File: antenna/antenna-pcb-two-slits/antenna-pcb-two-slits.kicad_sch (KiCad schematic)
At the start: 11 parts, among them J1 SMA Connector Male, U1 HHM1589D1

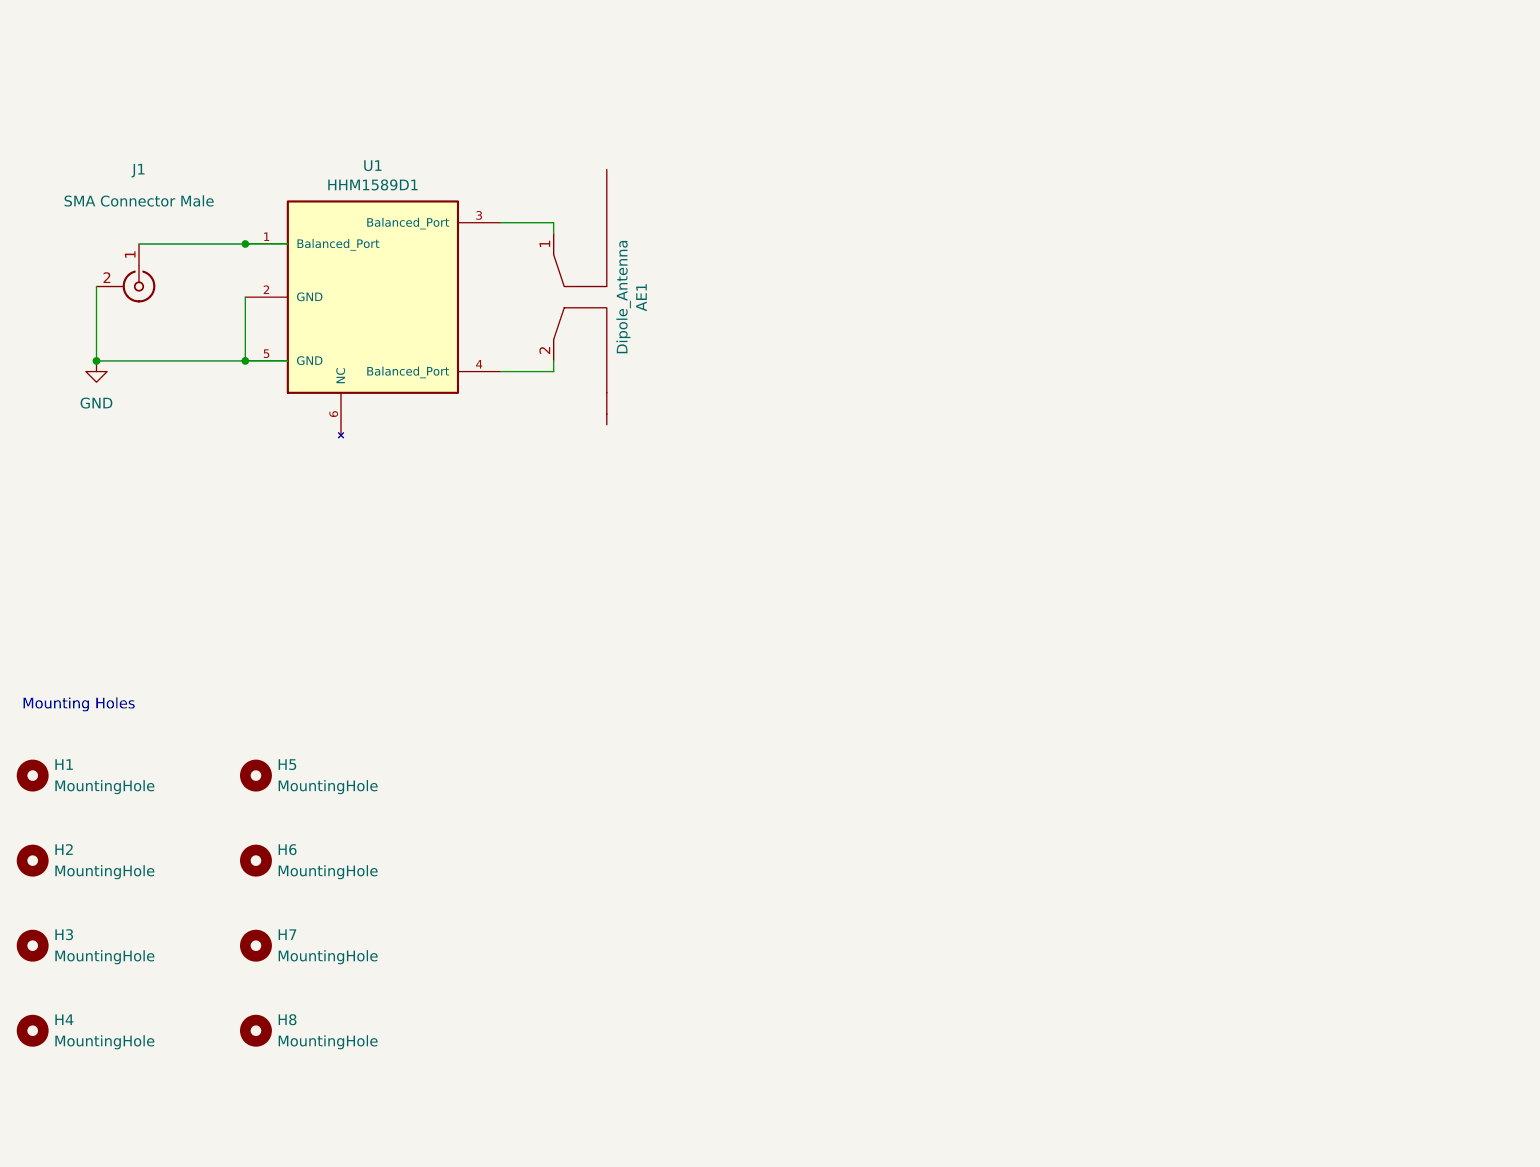
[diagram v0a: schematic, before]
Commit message: modify antenna pcbs and drc checked
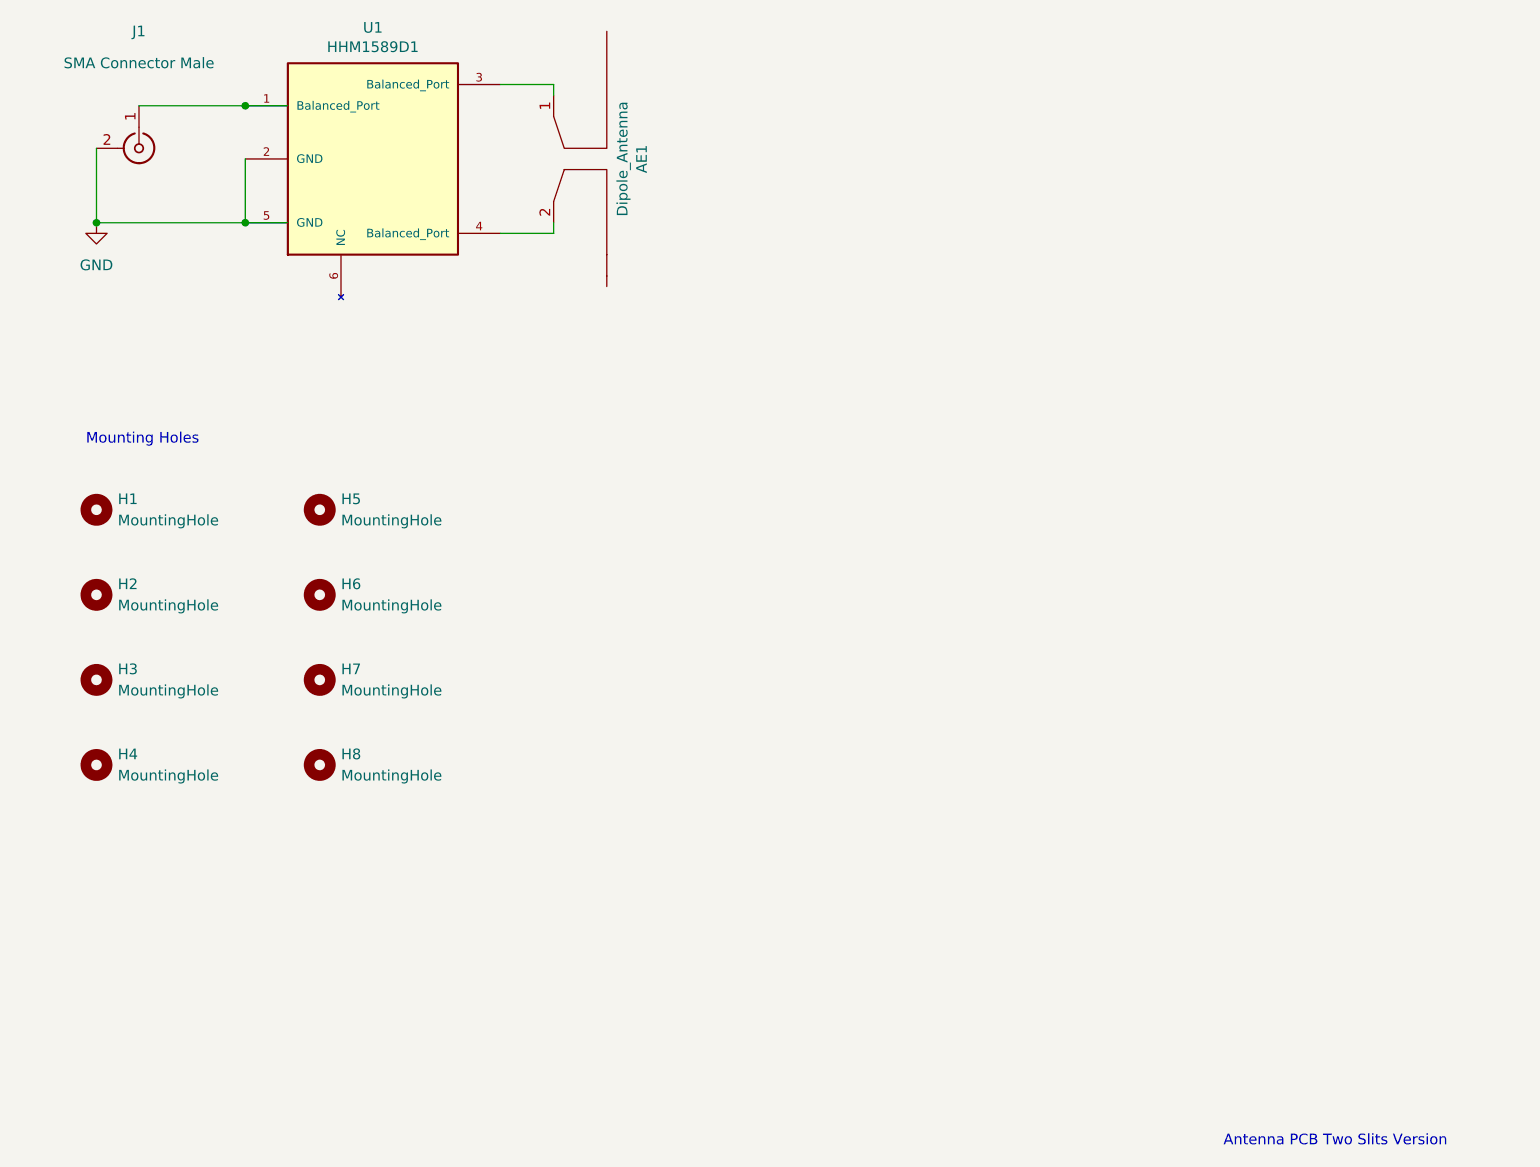
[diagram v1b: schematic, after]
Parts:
- AE1: footprint ISP:Antenna_Pads -> ISP:Antenna_Pads_Two_Slits
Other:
- note added: "Antenna PCB Two Slits Version"
- moved on the sheet: AE1, H1, H2, H3, H4, H5, H6, H7, H8, J1, U1
